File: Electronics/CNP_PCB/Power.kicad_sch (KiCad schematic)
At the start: 1 part, among them U3 TLV61070ADBV

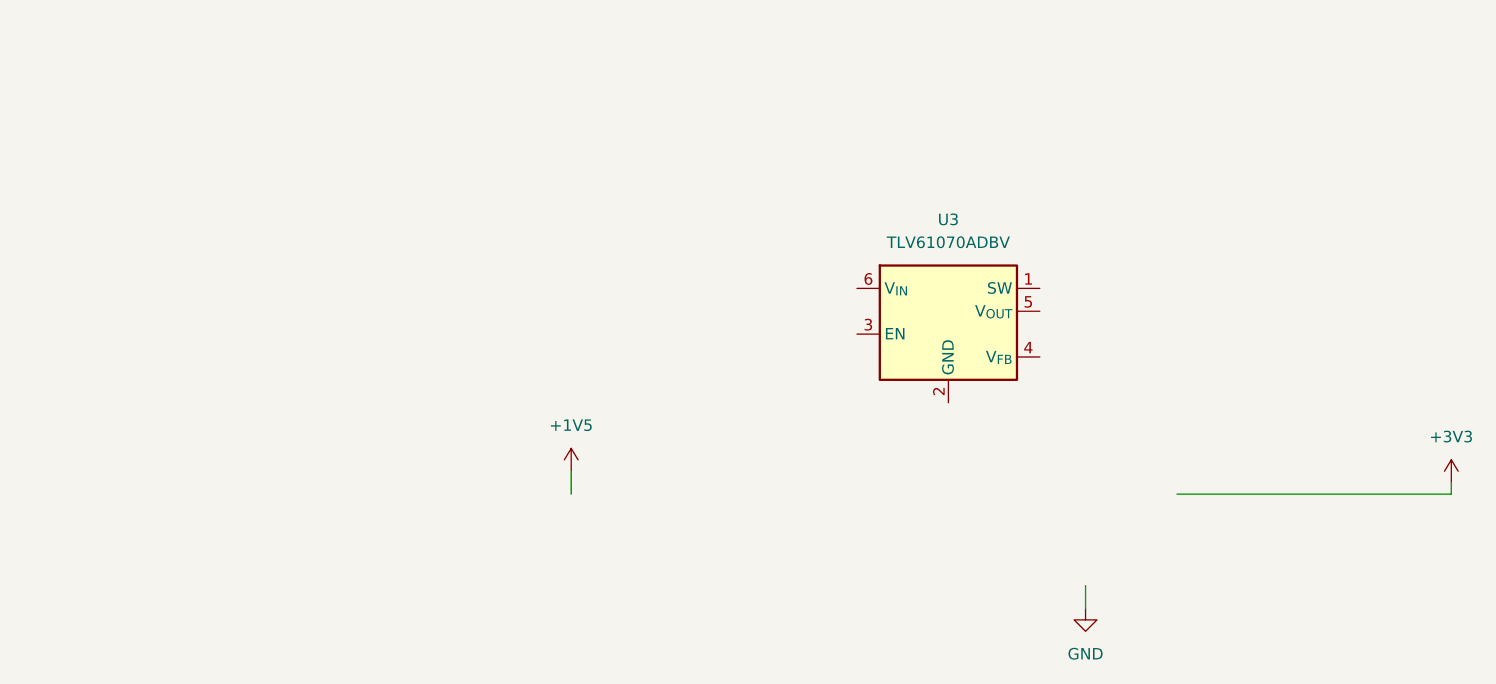
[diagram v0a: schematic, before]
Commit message: Latch circuit changes
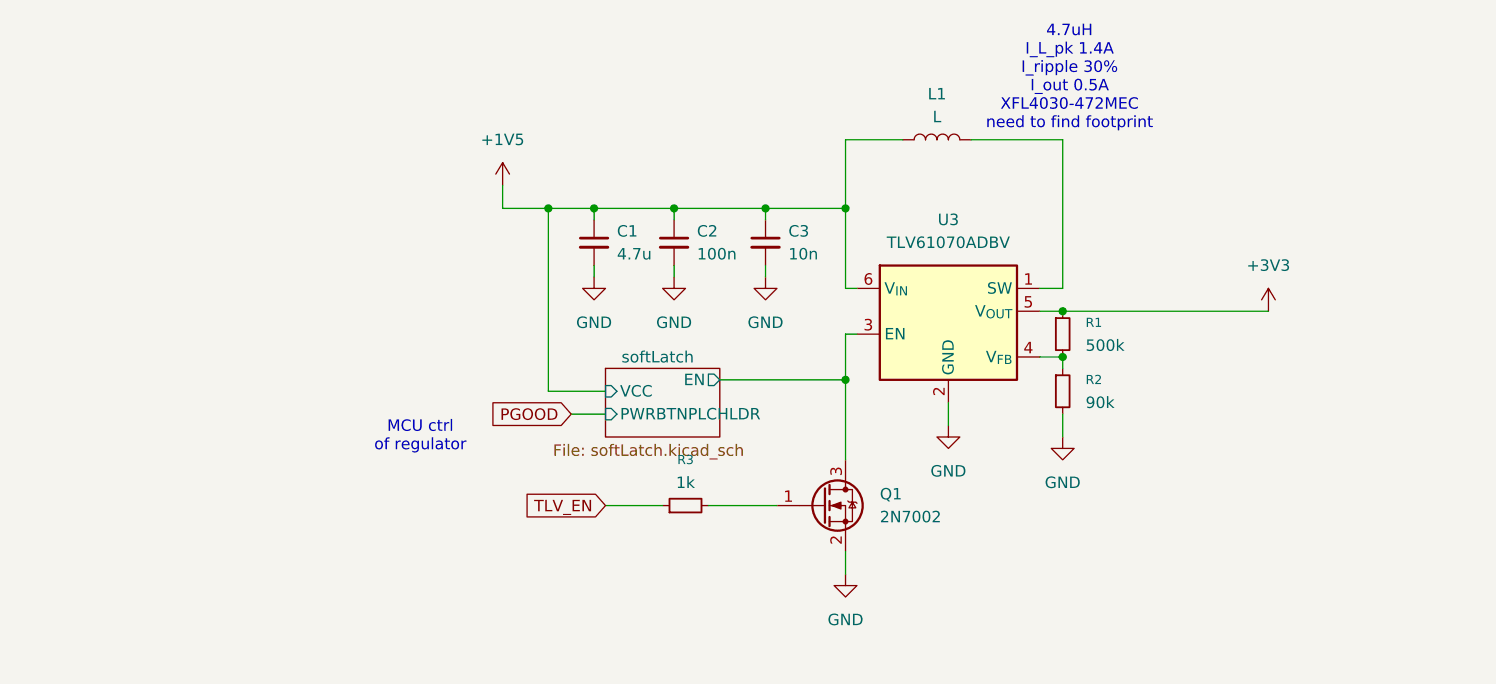
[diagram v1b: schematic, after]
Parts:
- added C1: 4.7u, Capacitor_SMD:C_0603_1608Metric, symbol Device:C_Small
- added C2: 100n, Capacitor_SMD:C_0603_1608Metric, symbol Device:C_Small
- added C3: 10n, Capacitor_SMD:C_0603_1608Metric, symbol Device:C_Small
- added L1: L, symbol Device:L
- added Q1: 2N7002, Package_TO_SOT_SMD:SOT-23, symbol Transistor_FET:2N7002
- added R1: 500k, Resistor_SMD:R_0603_1608Metric, symbol Device:R_Small
- added R2: 90k, Resistor_SMD:R_0603_1608Metric, symbol Device:R_Small
- added R3: 1k, Resistor_SMD:R_0603_1608Metric, symbol Device:R_Small
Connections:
- net +1V5: now also U3.6 (V_{IN}), C1.1, C2.1, C3.1, L1.1
- net +3V3: now also U3.5 (V_{OUT}), R1.1
- net GND: now also U3.2 (GND), C1.2, C2.2, C3.2, Q1.2 (S), R2.2
- net at U3.1 (SW): now also L1.2
- net softLatch/EN: now reaches U3.3 (EN)
- net softLatch/EN: now also Q1.3 (D)
- net at U3.4 (V_{FB}): now also R1.2, R2.1
- new net: Q1.1 (G), R3.2
- new net TLV_EN: R3.1
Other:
- added sheet softLatch (softLatch.kicad_sch)
- note added: "4.7uH I_L_pk 1.4A I_ripple 30% I_out 0.5A XFL4030-472MEC need to find footprint"
- note added: "MCU ctrl of regulator"

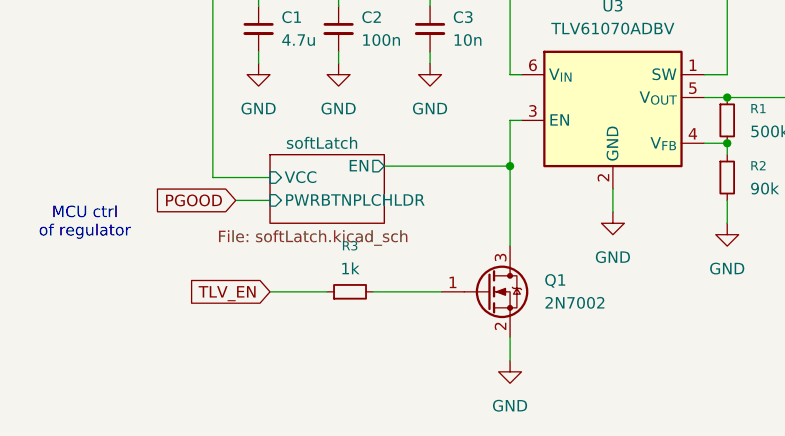
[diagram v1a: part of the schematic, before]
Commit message: finished softLatch circuit
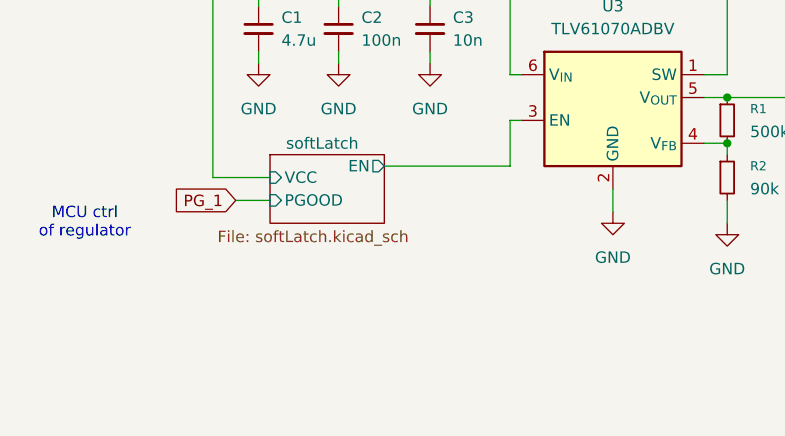
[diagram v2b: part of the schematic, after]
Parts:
- removed Q1: 2N7002, Package_TO_SOT_SMD:SOT-23, symbol Transistor_FET:2N7002
- removed R3: 1k, Resistor_SMD:R_0603_1608Metric, symbol Device:R_Small
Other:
- sheet softLatch ports: added PGOOD; removed PWRBTNPLCHLDR

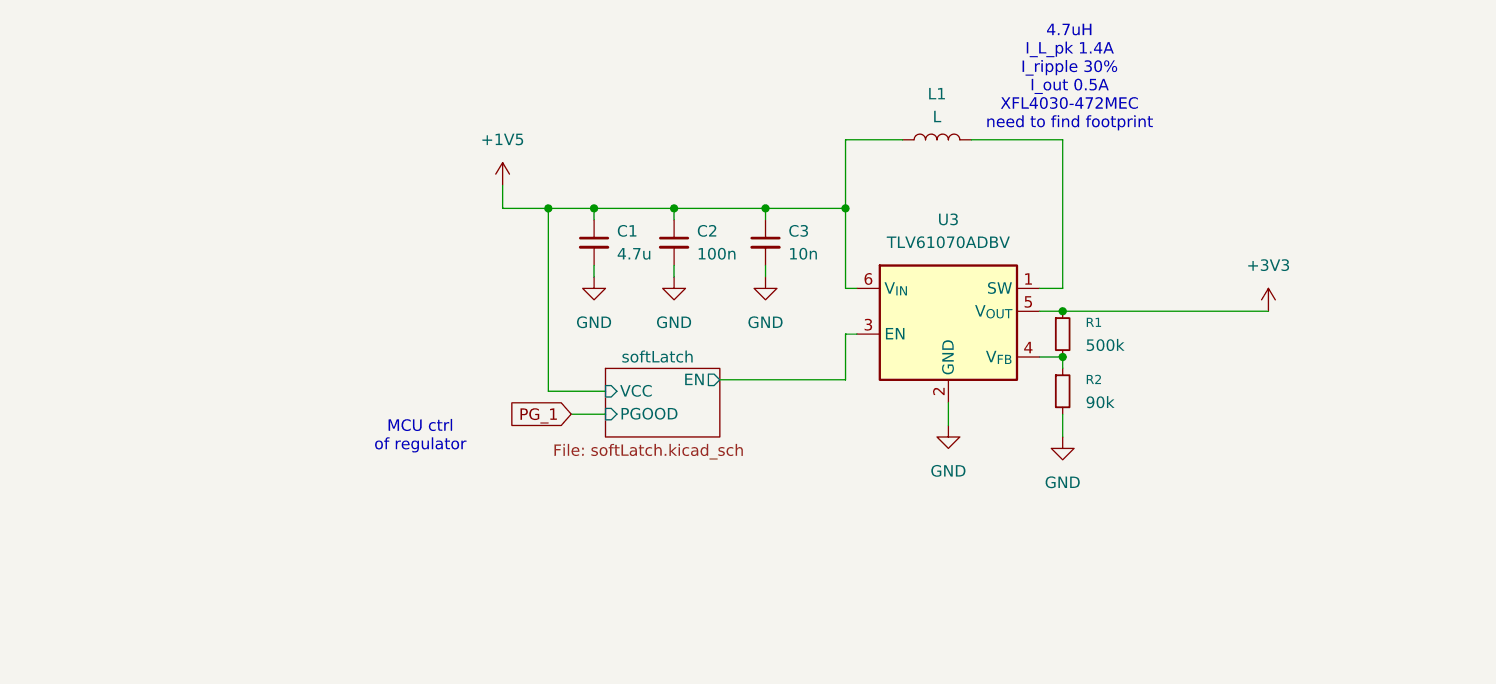
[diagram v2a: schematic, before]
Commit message: added switch logic for emulating buttons
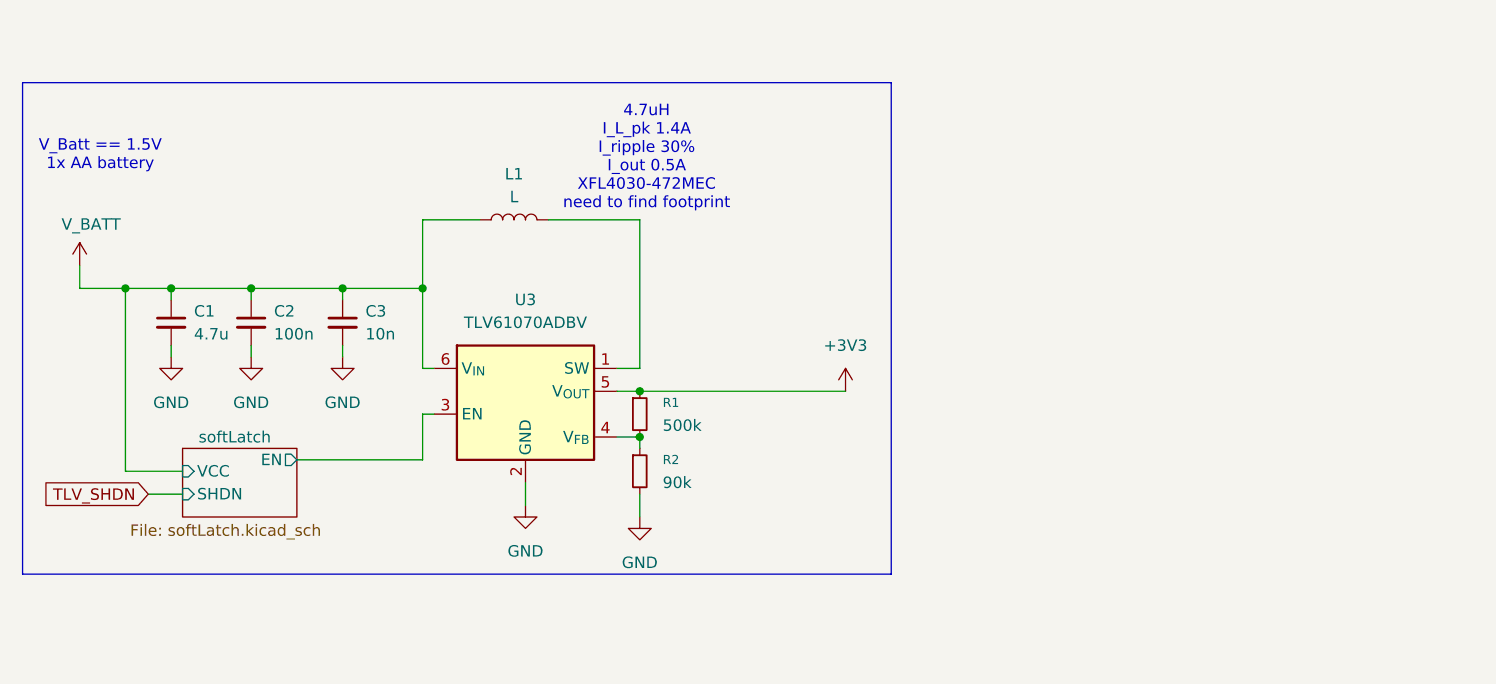
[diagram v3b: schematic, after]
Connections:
- net +1V5 renamed V_BATT
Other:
- sheet softLatch ports: added SHDN; removed PGOOD
- note added: "V_Batt == 1.5V 1x AA battery"
- note removed: "MCU ctrl of regulator"
- moved on the sheet: C1, C2, C3, L1, R1, R2, U3
